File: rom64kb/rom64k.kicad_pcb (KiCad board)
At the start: 2 copper layers, 81.3 x 65.3 mm, 3 parts, among them P1 CONN_02X25, U2 SST39SF010

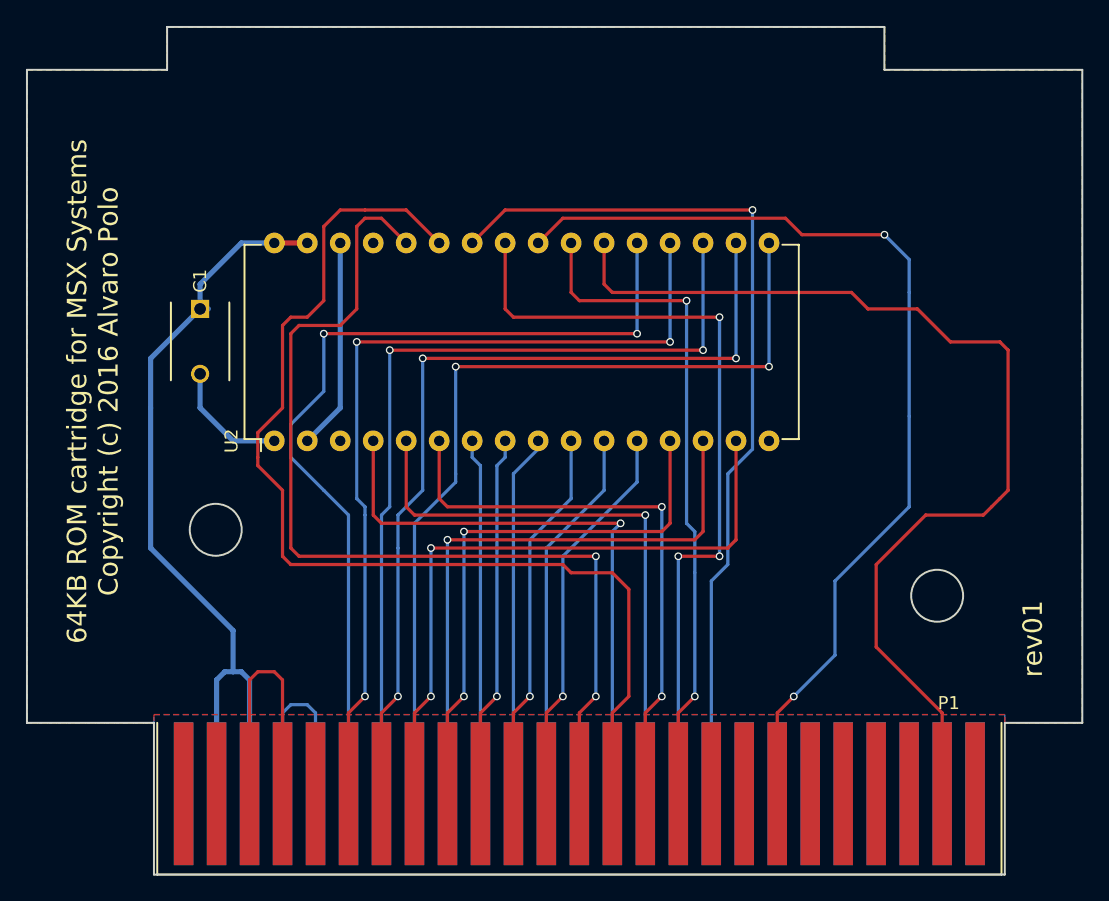
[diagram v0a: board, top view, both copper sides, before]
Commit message: Fix missing tracks in ROM 64KB
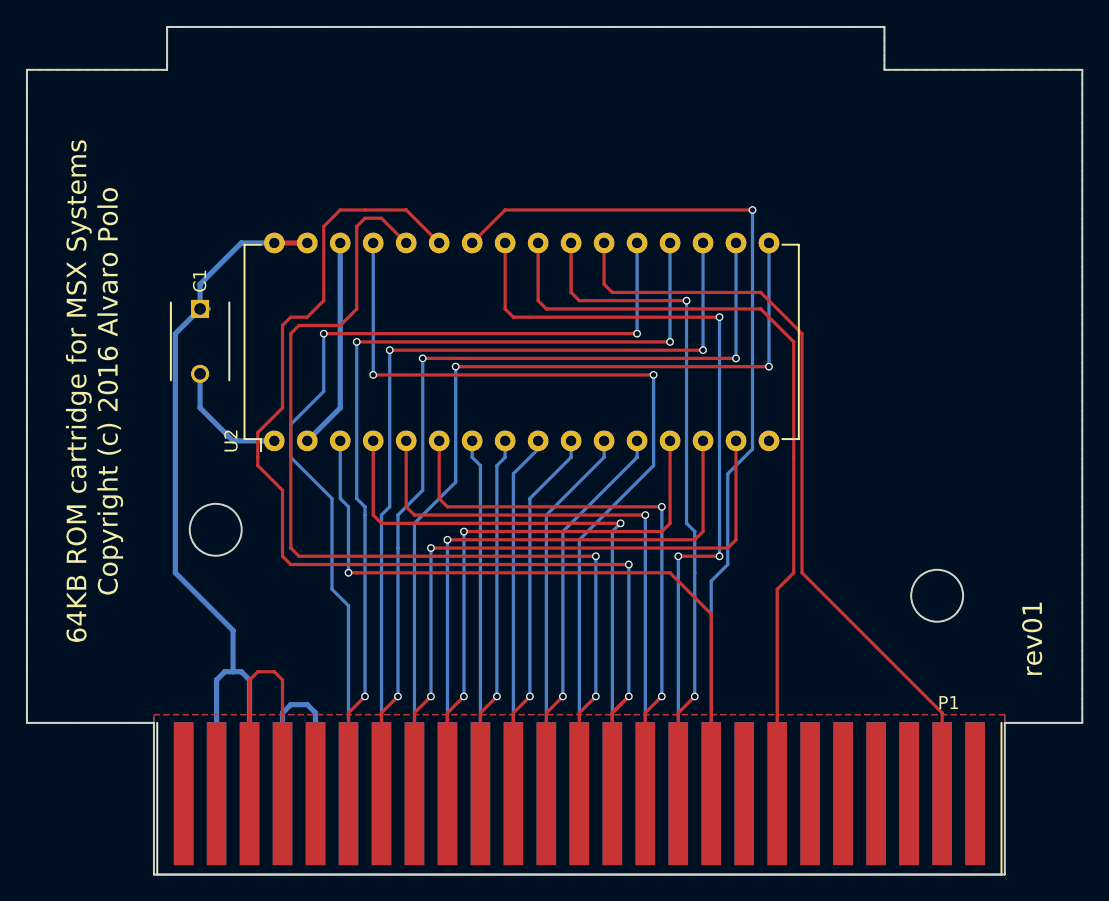
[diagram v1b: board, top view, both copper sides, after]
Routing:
- net /A14: track 0.00 -> 66.4 mm, vias 0 -> 2
- net /A15: track 0.00 -> 53.5 mm, vias 0 -> 1
- net ~SLTSL: track 79.5 -> 59.9 mm
- net ~RD: track 76.0 -> 60.8 mm, vias 2 -> 0
- net /A8: track 83.5 -> 92.6 mm, vias 0 -> 2
- net VCC: track 64.9 -> 63.3 mm
